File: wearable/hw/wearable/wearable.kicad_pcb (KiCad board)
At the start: 4 copper layers, 81.5 x 38 mm, 128 parts, among them IC1 LM4041CILPR, J1 USBC Charger, J2 Conn_02x05_Odd_Even, SW1 SW_Toggle, U1 ADS1299IPAG, U2 nRF54L15-QFXX, U3 BNO080, U4 nPM1300-QEXX, U5 LT3042xMSE, U6 TPS61040DBV, Y1 32.768kHz, Y2 32.768kHz, Y3 32MHz

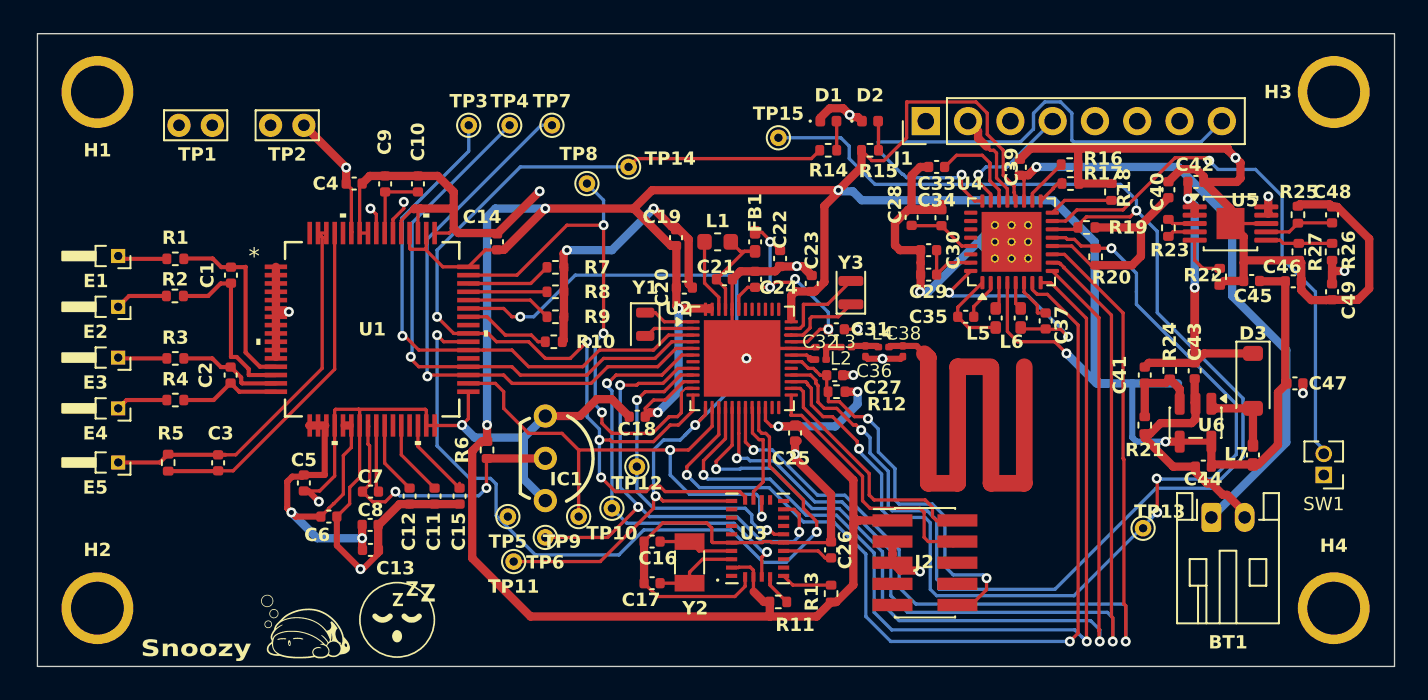
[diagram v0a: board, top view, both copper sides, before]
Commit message: BL54L15 added
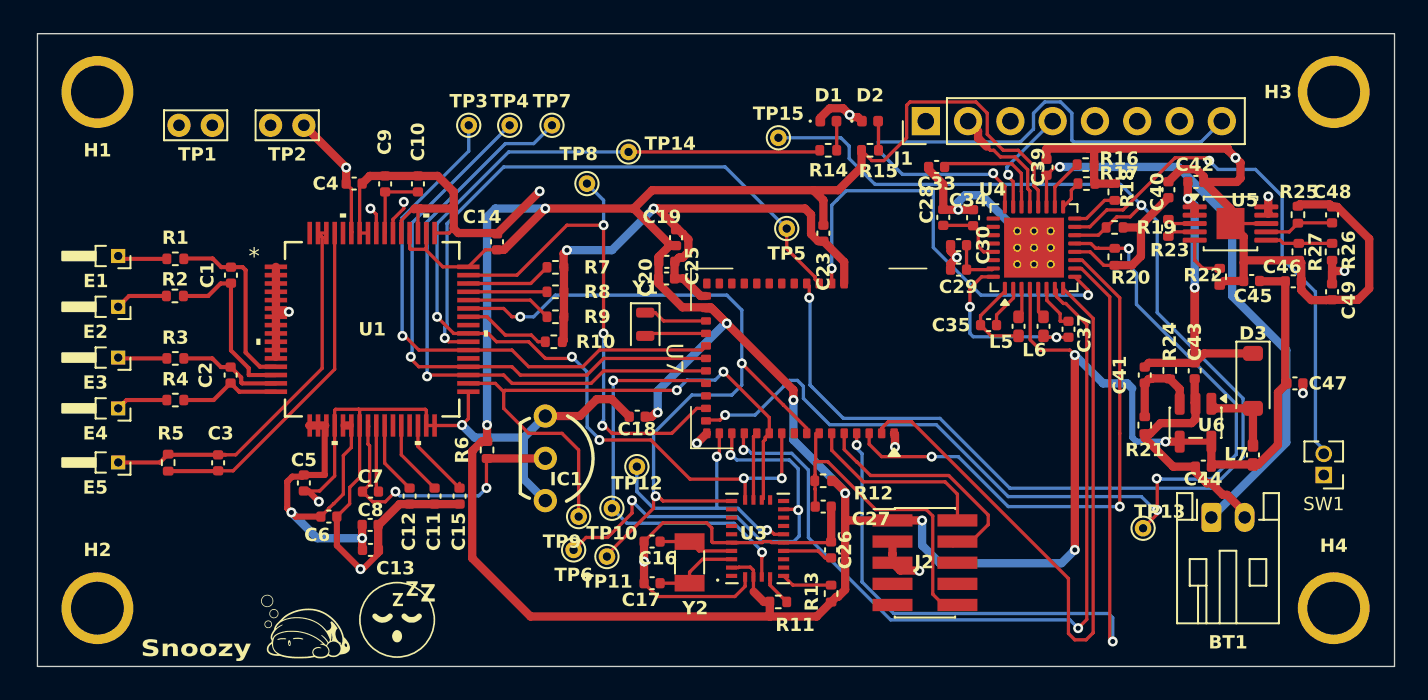
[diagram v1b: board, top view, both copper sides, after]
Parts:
- removed C21: 2.2uF, Capacitor_SMD:C_0402_1005Metric
- removed C22, C31: 2.2nF, Capacitor_SMD:C_0402_1005Metric
- removed C24: 10nF, Capacitor_SMD:C_0402_1005Metric
- removed C32: 1.5pF, Capacitor_SMD:C_0201_0603Metric
- removed C36: 2pF, Capacitor_SMD:C_0201_0603Metric
- removed C38: 0.3pF, Capacitor_SMD:C_0201_0603Metric
- removed FB1: FerriteBead, Inductor_SMD:L_0402_1005Metric_Pad0.77x0.64mm_HandSolder
- removed L1: 4.7nH, Inductor_SMD:L_0603_1608Metric
- removed L2, L4: 2.7nH, Inductor_SMD:L_0201_0603Metric
- removed L3: 3.5nH, Inductor_SMD:L_0201_0603Metric
- removed U2: nRF54L15-QFXX, Package_DFN_QFN:QFN-48-1EP_6x6mm_P0.4mm_EP4.6x4.6mm
- removed Y3: 32MHz, Unknown:Crystal_SMD_2016-2Pin_2.0x1.6mm
- added U7: BL54L15-453-000xxx, PCM_nordic-lib-kicad-nrf54-modules:BL54Lxx-LGA-39_14x10mm, F.Cu at (155.7, 102.0)
- moved TP5 24.1 mm to (154.0, 94.2)
- moved C25 12.8 mm to (146.8, 96.2), turned to 0 degrees
- moved C27 7.92 mm to (156.2, 110.9)
- moved TP11 5.61 mm to (143.2, 113.9)
- moved R12 5.41 mm to (156.2, 109.3)
- moved C23 3.10 mm to (156.2, 94.5), turned to -90 degrees
- moved C28 1.90 mm to (163.4, 93.5)
- moved C34 1.90 mm to (165.2, 93.5)
- moved TP6 1.86 mm to (141.2, 113.5)
- moved C29 1.82 mm to (164.3, 96.7)
- moved C30 1.82 mm to (164.3, 95.2)
- moved R19 1.69 mm to (173.7, 94.1)
- moved C39 1.60 mm to (169.6, 90.5)
- moved C35 1.46 mm to (166.1, 100.0)
- moved C37 1.46 mm to (170.9, 100.2)
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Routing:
- net RF: track 36.9 -> 0.00 mm
- net GPIO2: track 57.1 -> 26.5 mm
- net GPIO4: track 58.2 -> 33.4 mm
- net Net-(U2-DECA): track 15.7 -> 0.00 mm, vias 4 -> 0
- net GPIO1: track 56.9 -> 42.1 mm, vias 2 -> 0
- net AVSS: track 242.9 -> 228.8 mm, vias 17 -> 15
- net +3V3: track 225.1 -> 212.2 mm, vias 9 -> 10
- net CS_ADS1299: track 46.6 -> 35.9 mm, vias 2 -> 1
- net GPIO0: track 57.4 -> 49.6 mm
- net GPIO3: track 57.1 -> 50.0 mm
- net Net-(U2-DECD): track 6.75 -> 0.00 mm
- net SCL: track 87.7 -> 81.9 mm
- net Net-(U2-XC2): track 5.69 -> 0.00 mm
- net Net-(U2-XC1): track 5.03 -> 0.00 mm
- net INT_BNO085: track 31.9 -> 27.1 mm
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
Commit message: Ready for design review
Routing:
- net +3V3: track 212.2 -> 207.3 mm, vias 10 -> 8
- net GPIO3: track 50.0 -> 45.6 mm, vias 2 -> 0
- net INT_BNO085: track 27.1 -> 23.0 mm, vias 3 -> 2
- net MISO: track 48.0 -> 44.0 mm, vias 3 -> 4
- net RST_BNO085: track 15.9 -> 19.4 mm, vias 2 -> 1
- net SCK: track 61.2 -> 64.4 mm
- net +5V3: track 23.5 -> 20.6 mm
- net SDA: track 58.9 -> 56.8 mm
- net GPIO2: track 26.5 -> 27.6 mm
- net AVSS: track 228.8 -> 229.7 mm
- net BOOT_BNO085: track 25.0 -> 24.5 mm

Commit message: Checking with Alex
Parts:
- removed C29, C30, C34, C37: 10uF, Capacitor_SMD:C_0402_1005Metric
- removed L6: 2.2uH, Inductor_SMD:L_0402_1005Metric_Pad0.77x0.64mm_HandSolder
- removed R18: 150k, Resistor_SMD:R_0402_1005Metric
- C28: value 10uF -> 1uF
- moved C28 2.61 mm to (164.5, 95.9), turned to -90 degrees
- moved C35 1.20 mm to (167.0, 99.2)
- moved L5 0.76 mm to (167.2, 100.3), turned to 0 degrees
- moved R20 0.70 mm to (173.7, 95.2), turned to 180 degrees
- moved R22 0.21 mm to (180.1, 96.9)
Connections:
- C35 pad 1: Net-(U4-VOUT1) -> +3V3
- C35 pad 2: Net-(U4-PVSS1) -> AVSS
- C40 pad 2: VDDIO -> +3V3
- L5 pad 1: Net-(U4-VOUT1) -> +3V3
- R19 pad 1: VDDIO -> +3V3
- R20 pad 1: VDDIO -> +3V3
- R23 pad 1: Net-(U5-EN/UV) -> +5V3
- U4 pad 1: Net-(U4-VOUT1) -> +3V3
- U4 pad 12: VDDIO -> +3V3
- U4 pad 16: Net-(U4-VSET2) -> AVSS
- U4 pad 2: Net-(U4-PVSS1) -> AVSS
- U4 pad 30: VINLDO2 -> AVSS
- U4 pad 31: Net-(U4-LSOUT2/VOUTLDO2) -> AVSS
- U4 pad 32: Net-(U4-VOUT2) -> +3V3
- U4 pad 5: Net-(U4-SW2) -> unconnected-(U4-SW2-Pad5)
- U4 pad 6: Net-(U4-PVSS2) -> AVSS
- U5 pad 3: Net-(U5-EN/UV) -> +5V3
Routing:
- net +3V3: track 207.3 -> 234.3 mm
- net Net-(U4-VOUT2): track 11.2 -> 0.00 mm, vias 2 -> 0
- net VDDIO: track 9.66 -> 0.00 mm
- net Net-(U4-VOUT1): track 5.21 -> 0.00 mm
- net SDA: track 56.8 -> 51.8 mm
- net SCL: track 81.9 -> 78.0 mm
- net Net-(U4-LSOUT2/VOUTLDO2): track 3.10 -> 0.00 mm
- net Net-(U4-VSET2): track 2.65 -> 0.00 mm
- net Net-(U4-PVSS2): track 2.64 -> 0.00 mm
- net Net-(U4-PVSS1): track 2.47 -> 0.00 mm
- net Net-(U4-LSOUT1/VOUTLDO1): track 4.23 -> 1.97 mm
- net Net-(U4-SHPHLD): track 31.8 -> 30.1 mm
- net Net-(U5-EN/UV): track 1.68 -> 0.00 mm
- net +5V3: track 20.6 -> 22.3 mm
- net Net-(U4-SW2): track 1.67 -> 0.00 mm
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
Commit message: Almost done with design review...
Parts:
- removed C18, C20, C23, C25: 100nF, Capacitor_SMD:C_0402_1005Metric
- removed C19, C47: 10uF, Capacitor_SMD:C_0402_1005Metric
- removed C28: 1uF, Capacitor_SMD:C_0402_1005Metric
- removed J1: USBC Charger, Connector_PinHeader_2.54mm:PinHeader_1x08_P2.54mm_Vertical
- added C21: 1uF, Capacitor_SMD:C_0402_1005Metric, F.Cu at (119.4, 110.2)
- added J3: USB-C Connector, Connector_PinHeader_2.54mm:PinHeader_1x08_P2.54mm_Vertical, F.Cu at (162.2, 87.5)
- added R18: 10K, Resistor_SMD:R_0402_1005Metric, F.Cu at (117.4, 110.2)
- R17: value 47k -> 250k
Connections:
- C45 pad 1: +3V3 -> VSYS
- C46 pad 1: +3V3 -> VSYS
- E5 pad 1: Net-(U1-BIASIN) -> Net-(E5-Pad1)
- L5 pad 2: Net-(U4-SW1) -> Net-(U4-SW2)
- R17 pad 1: Net-(U4-VSET1) -> Net-(U4-VSET2)
- U4 pad 1: +3V3 -> VSYS
- U4 pad 16: AVSS -> Net-(U4-VSET2)
- U4 pad 17: Net-(U4-VSET1) -> AVSS
- U4 pad 20: +3V3 -> VSYS
- U4 pad 24: Net-(J1-Pin_8) -> AVSS
- U4 pad 28: VINLDO1 -> AVSS
- U4 pad 29: Net-(U4-LSOUT1/VOUTLDO1) -> AVSS
- U4 pad 3: Net-(U4-SW1) -> unconnected-(U4-SW1-Pad3)
- U4 pad 30: AVSS -> +3V3
- U4 pad 31: AVSS -> Net-(U4-LSOUT2/VOUTLDO2)
- U4 pad 4: +3V3 -> VSYS
- U4 pad 5: unconnected-(U4-SW2-Pad5) -> Net-(U4-SW2)
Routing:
- net AVSS: track 229.8 -> 268.6 mm, vias 14 -> 15
- net Net-(J1-Pin_8): track 35.1 -> 0.00 mm, vias 1 -> 0
- net Net-(U4-SW1): track 2.64 -> 0.00 mm
- net (no net): track 0.00 -> 2.64 mm
- net Net-(U4-LSOUT1/VOUTLDO1): track 1.97 -> 0.00 mm
- net Net-(U4-VSET1): track 1.77 -> 0.00 mm
- net +3V3: track 234.3 -> 232.9 mm

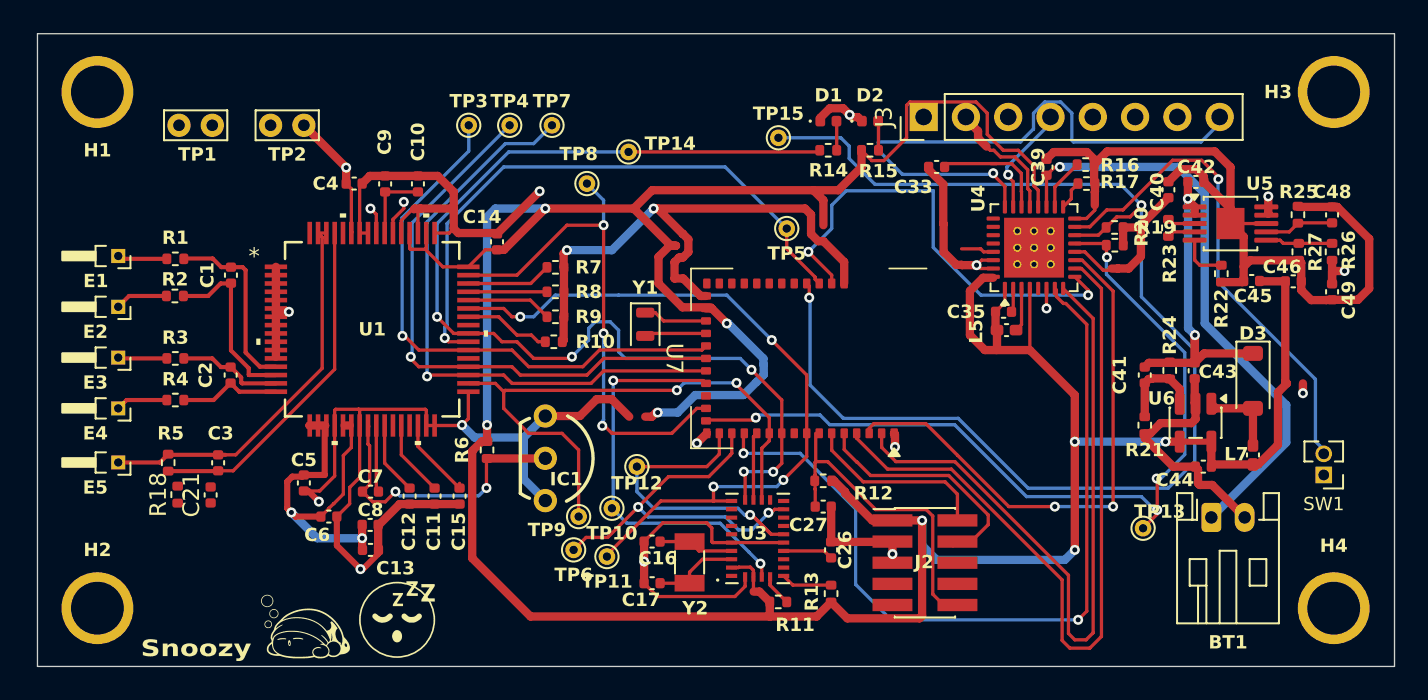
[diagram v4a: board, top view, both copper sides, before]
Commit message: Layed out design review changes
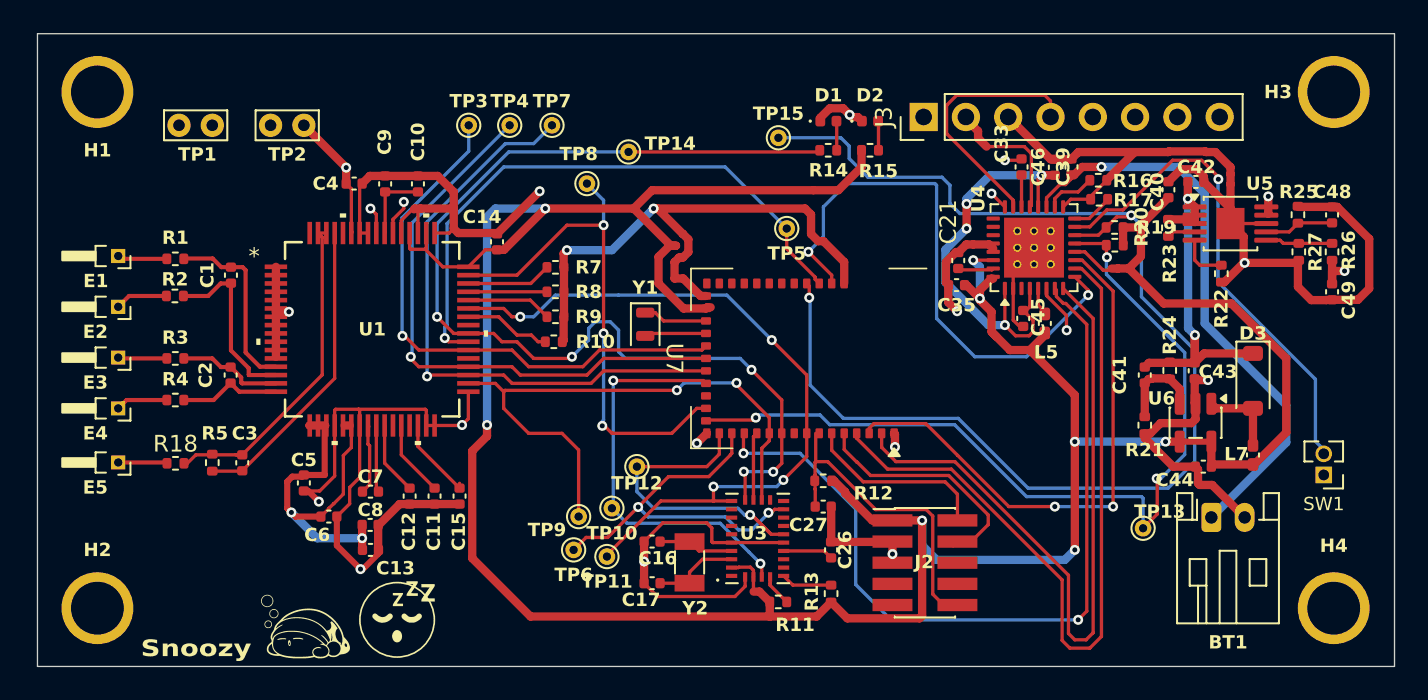
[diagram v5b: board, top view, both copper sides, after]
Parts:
- removed IC1: LM4041CILPR, ECE445L:ti_LM4041CILPR
- removed R6: 5.1K, Resistor_SMD:R_0402_1005Metric
- moved C21 47.1 mm to (164.3, 96.1)
- moved C46 15.9 mm to (170.1, 90.5), turned to 90 degrees
- moved C45 13.9 mm to (168.2, 99.6), turned to -90 degrees
- moved C33 5.10 mm to (168.1, 90.5), turned to 90 degrees
- moved C35 3.24 mm to (164.2, 97.6), turned to 180 degrees
- moved R5 2.65 mm to (119.5, 108.3)
- moved L5 2.33 mm to (169.5, 99.9), turned to 90 degrees
- moved R18 1.88 mm to (117.3, 108.3), turned to 0 degrees
- moved C39 1.50 mm to (171.1, 90.5)
- moved C3 1.45 mm to (121.3, 108.3)
- moved R16 1.21 mm to (172.7, 91.3)
- moved R17 1.21 mm to (172.8, 92.4), turned to 180 degrees
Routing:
- net AVSS: track 268.6 -> 222.7 mm, vias 15 -> 17
- net +3V3: track 232.9 -> 194.4 mm
- net VSYS: track 0.00 -> 25.6 mm, vias 0 -> 4
- net Net-(U1-VREFP): track 17.8 -> 4.27 mm, vias 2 -> 0
- net Net-(J3-Pin_4): track 6.45 -> 15.3 mm, vias 1 -> 0
- net GPIO2: track 27.6 -> 34.0 mm
- net Net-(U4-VBUSOUT): track 7.31 -> 1.92 mm
- net Net-(U1-BIASIN): track 23.4 -> 20.0 mm
- net Net-(E5-Pad1): track 0.00 -> 2.95 mm
- net (no net): track 2.64 -> 0.00 mm
- net Net-(U4-VSET2): track 0.00 -> 2.48 mm
- net Net-(U1-BIASINV): track 20.7 -> 18.4 mm
- net Net-(U4-LSOUT2/VOUTLDO2): track 0.00 -> 2.17 mm
- net Net-(U4-SW2): track 0.00 -> 1.69 mm
- net SCL: track 78.0 -> 77.1 mm
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
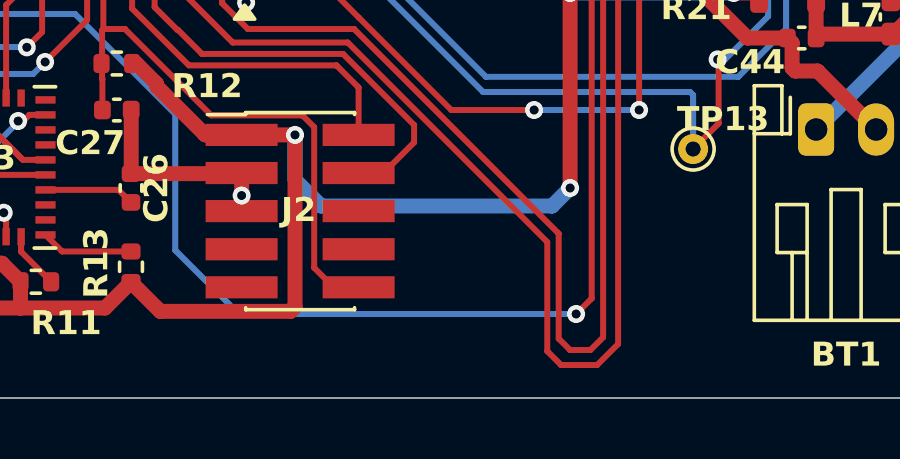
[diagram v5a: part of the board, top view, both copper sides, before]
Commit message: ESD protection, cyton reference, silkscreen update
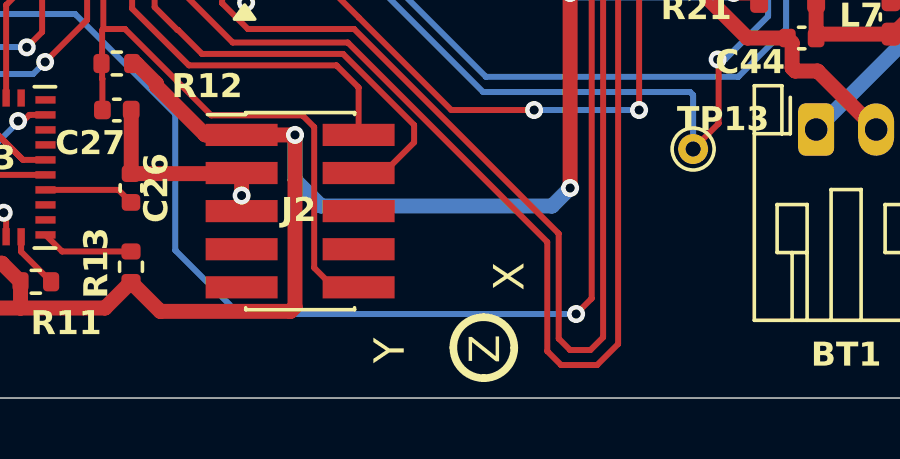
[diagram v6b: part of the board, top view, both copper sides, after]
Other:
- board text added: "X"
- board text added: "Y"
- board text added: "Z"
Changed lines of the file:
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@@
 		(embedded_fonts no)
 	)
+	(gr_arc
+		(start 168.423633 117.807633)
+		(mid 169.142053 118.105213)
+		(end 169.439633 118.823633)
+		(stroke
+			(width 0.254)
+			(type solid)
+		)
+		(layer "F.SilkS")
+	)
 	(gr_circle
 		(center 130.6 117.7)
@@
 		(layer "F.SilkS")
 	)
+	(gr_arc
+		(start 167.407633 118.823633)
+		(mid 167.7 118.1)
+		(end 168.423633 117.807633)
+		(stroke
+			(width 0.254)
+			(type solid)
+		)
+		(layer "F.SilkS")
+	)
+	(gr_arc
+		(start 169.439633 118.823633)
+		(mid 169.142053 119.542053)
+		(end 168.423633 119.839633)
+		(stroke
+			(width 0.254)
+			(type solid)
+		)
+		(layer "F.SilkS")
+	)
+	(gr_arc
+		(start 168.423633 119.839633)
+		(mid 167.705213 119.542053)
+		(end 167.407633 118.823633)
+		(stroke
+			(width 0.254)
+			(type solid)
+		)
+		(layer "F.SilkS")
+	)
 	(gr_rect
 		(start 109 82.5)
@@
 		(layer "User.1")
 	)
+	(gr_text "Y"
+		(at 165.881633 119.339633 90)
+		(layer "F.SilkS")
+		(effects
+			(font
+				(size 1.016 1.016)
+				(thickness 0.254)
+			)
+			(justify left bottom)
+		)
+	)
+	(gr_text "X"
+		(at 169.868893 116.921052 90)
+		(layer "F.SilkS")
+		(effects
+			(font
+				(size 1.016 1.016)
+				(thickness 0.254)
+			)
+			(justify left bottom)
+		)
+	)
 	(gr_text "Snoozy"
 		(at 115.2 120 0)
@@
 		)
 	)
+	(gr_text "Z"
+		(at 169.056633 119.339633 90)
+		(layer "F.SilkS")
+		(effects
+			(font
+				(size 1.016 1.016)
+				(thickness 0.254)
+			)
+			(justify left bottom)
+		)
+	)
 	(gr_text "ECE 464K: Aidan Aalund, Justin Bahn, Alex Ho, Kien Ton"
 		(at 167.5 120 0)
@@
 			)
 		)
+	)
+	(zone
+		(net 0)
+		(net_name "")
+		(layer "F.SilkS")
+		(hatch edge 0.5)
+		(priority 6)
+		(connect_pads
+			(clearance 0.000001)
+		)
+		(min_thickness 0.127)
+		(filled_areas_thickness no)
+		(fill
+			(thermal_gap 0.304)
+			(thermal_bridge_width 0.304)
+		)
+		(polygon
+			(pts
+				(xy 166.897633 118.196633) (xy 166.897633 118.577633) (xy 167.532633 118.577633) (xy 167.532633 119.085633)
+				(xy 166.897633 119.085633) (xy 166.897633 119.466633) (xy 166.050966 118.831633)
+			)
+		)
+	)
+	(zone
+		(net 0)
+		(net_name "")
+		(layer "F.SilkS")
+		(hatch edge 0.5)
+		(priority 6)
+		(connect_pads
+			(clearance 0.000001)
+		)
+		(min_thickness 0.127)
+		(filled_areas_thickness no)
+		(fill
+			(thermal_gap 0.304)
+			(thermal_bridge_width 0.304)
+		)
+		(polygon
+			(pts
+				(xy 168.423633 116.452966) (xy 169.058633 117.299633) (xy 168.677633 117.299633) (xy 168.677633 117.934633)
+				(xy 168.169633 117.934633) (xy 168.169633 117.299633) (xy 167.788633 117.299633)
+			)
+		)
